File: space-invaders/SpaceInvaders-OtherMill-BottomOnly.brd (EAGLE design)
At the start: 127 x 101.6 mm, 26 parts, among them J2-J4 TM4C123GXL, J3-J1 TM4C123GXL, J5 Nokia_5110, J6 Nokia_5110, J7 9V, U1 LM7805CT

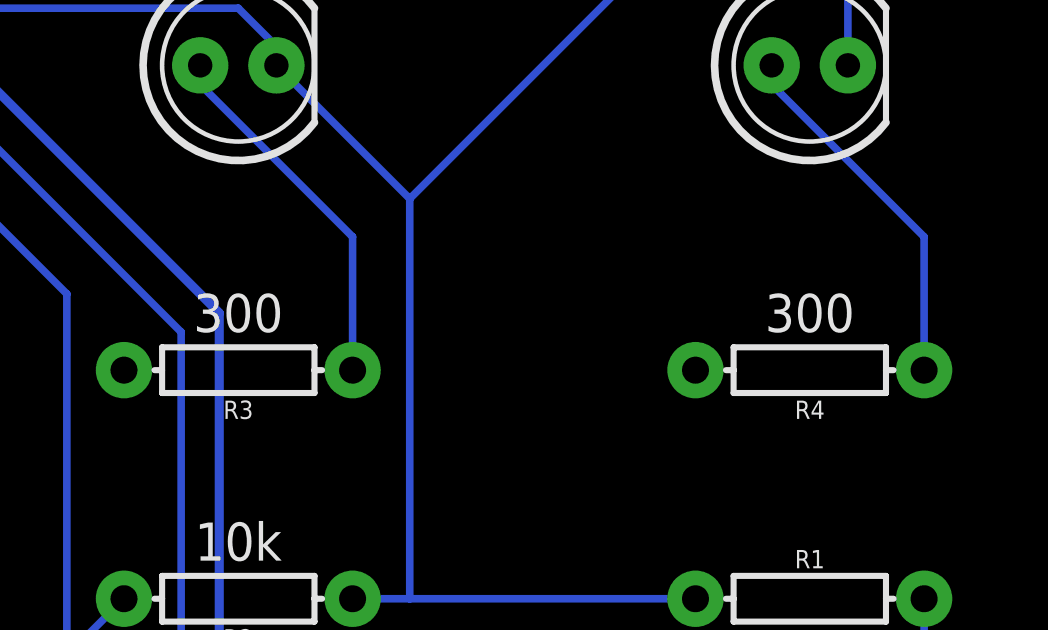
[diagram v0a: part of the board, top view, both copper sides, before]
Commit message: Change LLED and RLED resistor value from 300 to 220
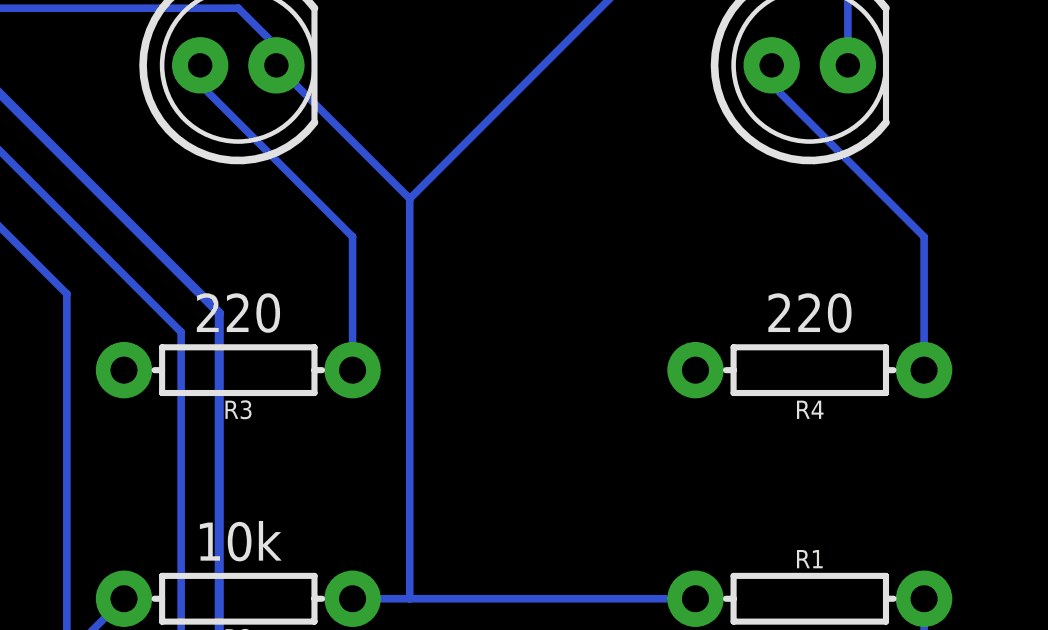
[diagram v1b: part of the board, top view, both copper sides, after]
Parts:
- D1: value YELLOW -> RED
- D2: value RED -> YELLOW
- R3, R4: value 300 -> 220
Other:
- board text removed: "300"
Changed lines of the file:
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@@
 <text x="110.617" y="76.835" size="1.27" layer="21" font="vector" ratio="10" align="center">-</text>
 <text x="78.74" y="82.55" size="1.27" layer="21" font="vector" align="top-center">220</text>
-<text x="93.98" y="30.48" size="1.27" layer="21" font="vector" align="top-center">300</text>
-<text x="113.03" y="30.48" size="1.27" layer="21" font="vector" align="top-center">300</text>
+<text x="93.98" y="30.48" size="1.27" layer="21" font="vector" align="top-center">220</text>
+<text x="113.03" y="30.48" size="1.27" layer="21" font="vector" align="top-center">220</text>
 <text x="93.98" y="21.59" size="1.27" layer="21" font="vector" rot="R180" align="top-center">10k</text>
 <text x="113.03" y="17.78" size="1.27" layer="21" font="vector" rot="R180" align="top-center">10k</text>
@@
 <attribute name="PROD_ID" value="CAP-08370" x="116.84" y="63.5" size="1.778" layer="27" display="off"/>
 </element>
-<element name="D1" library="SparkFun-LED" package="LED_5MM" value="YELLOW" x="93.98" y="38.1"/>
-<element name="D2" library="SparkFun-LED" package="LED_5MM" value="RED" x="113.03" y="38.1"/>
+<element name="D1" library="SparkFun-LED" package="LED_5MM" value="RED" x="93.98" y="38.1"/>
+<element name="D2" library="SparkFun-LED" package="LED_5MM" value="YELLOW" x="113.03" y="38.1"/>
 <element name="FRAME1" library="SparkFun-Aesthetics" package="CREATIVE_COMMONS" value="FRAME-LETTER" x="30.48" y="-8.89"/>
 <element name="J2-J4" library="SparkFun-Connectors" package="2X10" value="TM4C123GXL" x="48.26" y="66.04" rot="R270"/>
@@
 <attribute name="PROD_ID" value="RES-09435" x="93.98" y="20.32" size="1.778" layer="27" rot="R180" display="off"/>
 </element>
-<element name="R3" library="SparkFun-Resistors" package="AXIAL-0.3" value="300" x="93.98" y="27.94" rot="R180">
+<element name="R3" library="SparkFun-Resistors" package="AXIAL-0.3" value="220" x="93.98" y="27.94" rot="R180">
 <attribute name="PROD_ID" value="RES-08380" x="93.98" y="27.94" size="1.778" layer="27" rot="R180" display="off"/>
 </element>
-<element name="R4" library="SparkFun-Resistors" package="AXIAL-0.3" value="300" x="113.03" y="27.94" rot="R180">
+<element name="R4" library="SparkFun-Resistors" package="AXIAL-0.3" value="220" x="113.03" y="27.94" rot="R180">
 <attribute name="PROD_ID" value="RES-08380" x="113.03" y="27.94" size="1.778" layer="27" rot="R180" display="off"/>
 </element>
